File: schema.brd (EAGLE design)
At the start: 51.7 x 53.3 mm, 6 parts

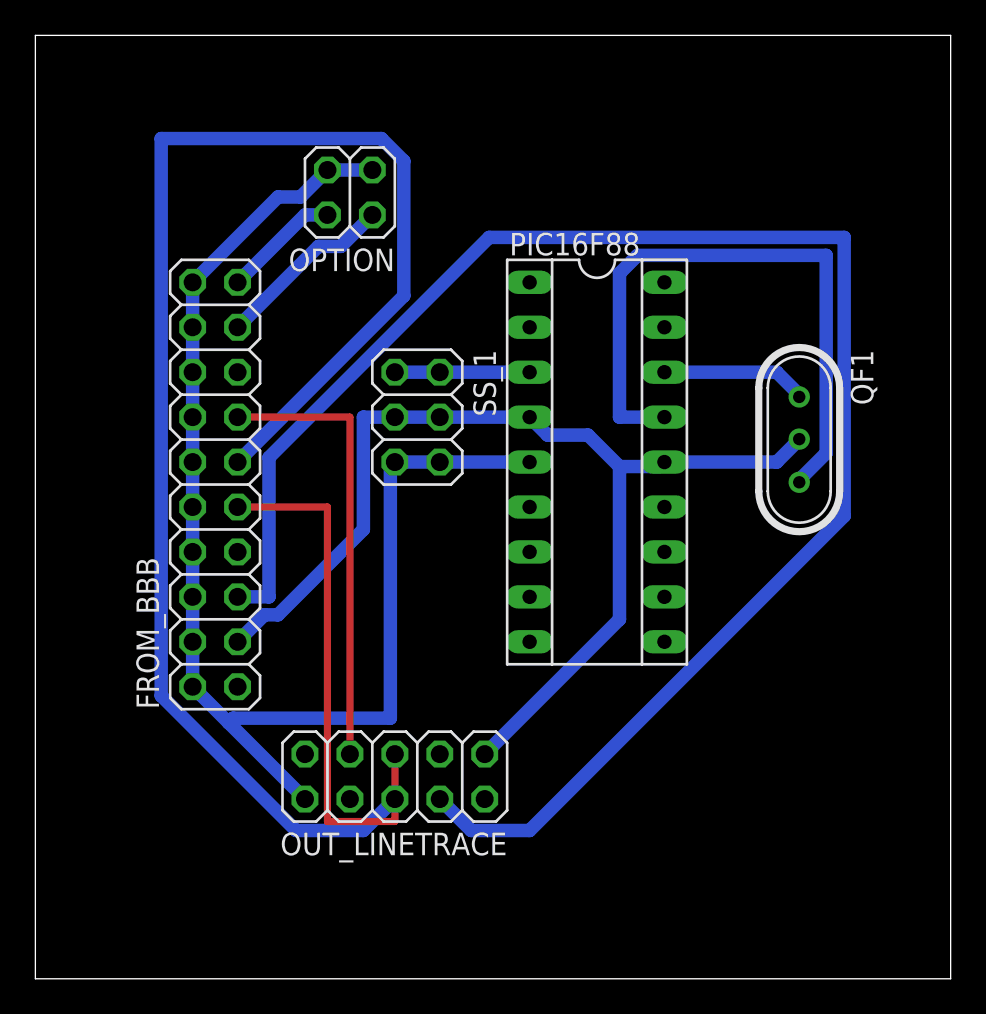
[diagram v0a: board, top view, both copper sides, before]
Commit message: trimmed the corners
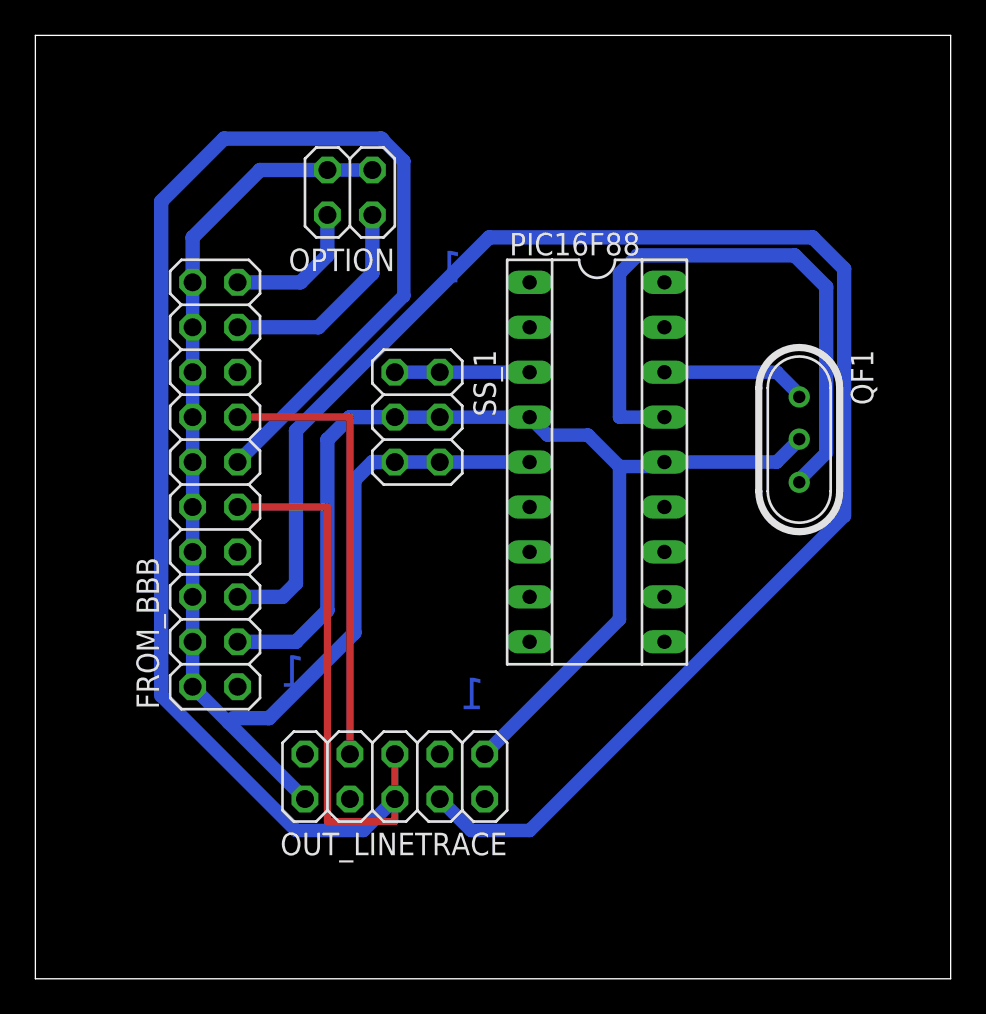
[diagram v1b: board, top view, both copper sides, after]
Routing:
- net N$3: track 83.7 -> 81.7 mm
- net N$6: track 62.0 -> 63.9 mm
- net N$10: track 10.3 -> 12.2 mm
- net GND: track 76.1 -> 74.3 mm
- net N$11: track 6.66 -> 8.00 mm
- net N$8: track 36.2 -> 35.2 mm
- net N$1: track 94.0 -> 93.4 mm
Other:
- board text added: "1"
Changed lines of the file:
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@@
 <setting verticaltext="up"/>
 </settings>
-<grid distance="0.05" unitdist="inch" unit="inch" style="dots" multiple="1" display="yes" altdistance="0.025" altunitdist="inch" altunit="inch"/>
+<grid distance="0.01" unitdist="inch" unit="inch" style="lines" multiple="1" display="yes" altdistance="0.025" altunitdist="inch" altunit="inch"/>
 <layers>
 <layer number="1" name="Top" color="4" fill="1" visible="yes" active="yes"/>
@@
 <wire x1="51.74" y1="53.33" x2="0" y2="53.33" width="0" layer="20"/>
 <wire x1="0" y1="53.33" x2="0" y2="0" width="0" layer="20"/>
+<text x="25.4" y="15.24" size="1.778" layer="16" rot="MR0">1</text>
+<text x="15.24" y="16.51" size="1.778" layer="16" rot="MR0">1</text>
+<text x="24.13" y="39.37" size="1.778" layer="16" rot="MR0">1</text>
 </plain>
 <attributes>
@@
 <wire x1="27.94" y1="8.382" x2="24.638" y2="8.382" width="0.762" layer="16"/>
 <wire x1="45.72" y1="26.162" x2="27.94" y2="8.382" width="0.762" layer="16"/>
-<wire x1="45.72" y1="41.91" x2="45.72" y2="26.162" width="0.762" layer="16"/>
-<wire x1="25.654" y1="41.91" x2="45.72" y2="41.91" width="0.762" layer="16"/>
-<wire x1="13.208" y1="29.464" x2="25.654" y2="41.91" width="0.762" layer="16"/>
-<wire x1="13.208" y1="21.59" x2="13.208" y2="29.464" width="0.762" layer="16"/>
-<wire x1="11.43" y1="21.59" x2="13.208" y2="21.59" width="0.762" layer="16"/>
+<wire x1="11.43" y1="21.59" x2="13.97" y2="21.59" width="0.8128" layer="16"/>
+<wire x1="13.97" y1="21.59" x2="14.732" y2="22.352" width="0.8128" layer="16"/>
+<wire x1="14.732" y1="22.352" x2="14.732" y2="30.988" width="0.8128" layer="16"/>
+<wire x1="14.732" y1="30.988" x2="25.654" y2="41.91" width="0.8128" layer="16"/>
+<wire x1="25.654" y1="41.91" x2="43.942" y2="41.91" width="0.8128" layer="16"/>
+<wire x1="43.942" y1="41.91" x2="45.72" y2="40.132" width="0.8128" layer="16"/>
+<wire x1="45.72" y1="40.132" x2="45.72" y2="26.162" width="0.8128" layer="16"/>
 </signal>
 <signal name="N$2">
@@
 <wire x1="14.732" y1="8.382" x2="18.542" y2="8.382" width="0.762" layer="16"/>
 <wire x1="7.112" y1="16.002" x2="14.732" y2="8.382" width="0.762" layer="16"/>
-<wire x1="7.112" y1="47.498" x2="7.112" y2="16.002" width="0.762" layer="16"/>
-<wire x1="19.558" y1="47.498" x2="7.112" y2="47.498" width="0.762" layer="16"/>
-<wire x1="20.828" y1="46.228" x2="19.558" y2="47.498" width="0.762" layer="16"/>
+<wire x1="20.828" y1="46.228" x2="19.685" y2="47.371" width="0.762" layer="16"/>
 <wire x1="20.828" y1="38.608" x2="20.828" y2="46.228" width="0.762" layer="16"/>
 <wire x1="11.43" y1="29.21" x2="20.828" y2="38.608" width="0.762" layer="16"/>
+<wire x1="7.112" y1="16.002" x2="7.112" y2="43.942" width="0.8128" layer="16"/>
+<wire x1="7.112" y1="43.942" x2="10.668" y2="47.498" width="0.8128" layer="16"/>
+<wire x1="10.668" y1="47.498" x2="19.558" y2="47.498" width="0.8128" layer="16"/>
+<wire x1="19.558" y1="47.498" x2="19.685" y2="47.371" width="0.8128" layer="16"/>
 </signal>
 <signal name="N$4">
@@
 <wire x1="8.89" y1="34.29" x2="8.89" y2="36.83" width="0.762" layer="16"/>
 <wire x1="8.89" y1="36.83" x2="8.89" y2="39.37" width="0.762" layer="16"/>
-<wire x1="14.986" y1="44.196" x2="16.51" y2="45.72" width="0.762" layer="16"/>
-<wire x1="13.716" y1="44.196" x2="14.986" y2="44.196" width="0.762" layer="16"/>
-<wire x1="8.89" y1="39.37" x2="13.716" y2="44.196" width="0.762" layer="16"/>
-<wire x1="20.066" y1="14.732" x2="20.066" y2="28.956" width="0.762" layer="16"/>
-<wire x1="11.176" y1="14.732" x2="20.066" y2="14.732" width="0.762" layer="16"/>
-<wire x1="20.066" y1="28.956" x2="20.32" y2="29.21" width="0.762" layer="16"/>
 <wire x1="11.176" y1="14.732" x2="10.922" y2="14.478" width="0.762" layer="16"/>
+<wire x1="8.89" y1="39.37" x2="8.89" y2="41.91" width="0.8128" layer="16"/>
+<wire x1="8.89" y1="41.91" x2="12.7" y2="45.72" width="0.8128" layer="16"/>
+<wire x1="12.7" y1="45.72" x2="16.51" y2="45.72" width="0.8128" layer="16"/>
+<wire x1="11.176" y1="14.732" x2="13.208" y2="14.732" width="0.8128" layer="16"/>
+<wire x1="13.208" y1="14.732" x2="18.034" y2="19.558" width="0.8128" layer="16"/>
+<wire x1="18.034" y1="19.558" x2="18.034" y2="28.194" width="0.8128" layer="16"/>
+<wire x1="18.034" y1="28.194" x2="19.05" y2="29.21" width="0.8128" layer="16"/>
+<wire x1="19.05" y1="29.21" x2="20.32" y2="29.21" width="0.8128" layer="16"/>
 </signal>
 <signal name="N$6">
@@
 <contactref element="SS_1" pad="3"/>
 <wire x1="22.86" y1="31.75" x2="27.94" y2="31.75" width="0.762" layer="16"/>
-<wire x1="12.954" y1="20.574" x2="11.43" y2="19.05" width="0.762" layer="16"/>
-<wire x1="13.716" y1="20.574" x2="12.954" y2="20.574" width="0.762" layer="16"/>
-<wire x1="18.542" y1="25.4" x2="13.716" y2="20.574" width="0.762" layer="16"/>
-<wire x1="18.542" y1="31.75" x2="18.542" y2="25.4" width="0.762" layer="16"/>
-<wire x1="20.32" y1="31.75" x2="18.542" y2="31.75" width="0.762" layer="16"/>
 <wire x1="20.32" y1="31.75" x2="22.86" y2="31.75" width="0.762" layer="16"/>
 <wire x1="41.91" y1="29.21" x2="43.18" y2="30.48" width="0.762" layer="16"/>
@@
 <wire x1="31.242" y1="30.734" x2="28.956" y2="30.734" width="0.762" layer="16"/>
 <wire x1="33.02" y1="28.956" x2="31.242" y2="30.734" width="0.762" layer="16"/>
+<wire x1="11.43" y1="19.05" x2="14.732" y2="19.05" width="0.8128" layer="16"/>
+<wire x1="14.732" y1="19.05" x2="16.51" y2="20.828" width="0.8128" layer="16"/>
+<wire x1="16.51" y1="20.828" x2="16.51" y2="30.48" width="0.8128" layer="16"/>
+<wire x1="16.51" y1="30.48" x2="17.78" y2="31.75" width="0.8128" layer="16"/>
+<wire x1="17.78" y1="31.75" x2="20.32" y2="31.75" width="0.8128" layer="16"/>
 </signal>
 <signal name="N$7">
@@
 <contactref element="QF1" pad="3"/>
 <wire x1="44.704" y1="29.718" x2="43.18" y2="28.194" width="0.762" layer="16"/>
-<wire x1="44.704" y1="40.894" x2="44.704" y2="29.718" width="0.762" layer="16"/>
-<wire x1="34.036" y1="40.894" x2="44.704" y2="40.894" width="0.762" layer="16"/>
 <wire x1="33.02" y1="39.878" x2="34.036" y2="40.894" width="0.762" layer="16"/>
 <wire x1="33.02" y1="31.75" x2="33.02" y2="39.878" width="0.762" layer="16"/>
 <wire x1="35.56" y1="31.75" x2="33.02" y2="31.75" width="0.762" layer="16"/>
 <wire x1="43.18" y1="28.194" x2="43.18" y2="28.067" width="0.762" layer="16"/>
+<wire x1="34.036" y1="40.894" x2="42.926" y2="40.894" width="0.8128" layer="16"/>
+<wire x1="42.926" y1="40.894" x2="44.704" y2="39.116" width="0.8128" layer="16"/>
+<wire x1="44.704" y1="39.116" x2="44.704" y2="29.718" width="0.8128" layer="16"/>
 </signal>
 <signal name="N$5">
@@
 <contactref element="FROM_BBB" pad="17"/>
 <contactref element="OPTION" pad="2"/>
-<wire x1="16.002" y1="41.402" x2="11.43" y2="36.83" width="0.762" layer="16"/>
-<wire x1="17.272" y1="41.402" x2="16.002" y2="41.402" width="0.762" layer="16"/>
-<wire x1="19.05" y1="43.18" x2="17.272" y2="41.402" width="0.762" layer="16"/>
+<wire x1="11.43" y1="36.83" x2="16.002" y2="36.83" width="0.8128" layer="16"/>
+<wire x1="16.002" y1="36.83" x2="19.05" y2="39.878" width="0.8128" layer="16"/>
+<wire x1="19.05" y1="39.878" x2="19.05" y2="43.18" width="0.8128" layer="16"/>
 </signal>
 <signal name="N$11">
 <contactref element="FROM_BBB" pad="19"/>
 <contactref element="OPTION" pad="4"/>
-<wire x1="15.24" y1="43.18" x2="11.43" y2="39.37" width="0.762" layer="16"/>
-<wire x1="16.51" y1="43.18" x2="15.24" y2="43.18" width="0.762" layer="16"/>
+<wire x1="11.43" y1="39.37" x2="14.986" y2="39.37" width="0.8128" layer="16"/>
+<wire x1="14.986" y1="39.37" x2="16.51" y2="40.894" width="0.8128" layer="16"/>
+<wire x1="16.51" y1="40.894" x2="16.51" y2="43.18" width="0.8128" layer="16"/>
 </signal>
 </signals>

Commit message: add PDFs and correct wrong wiring from Crystal Generator to SYS_5V
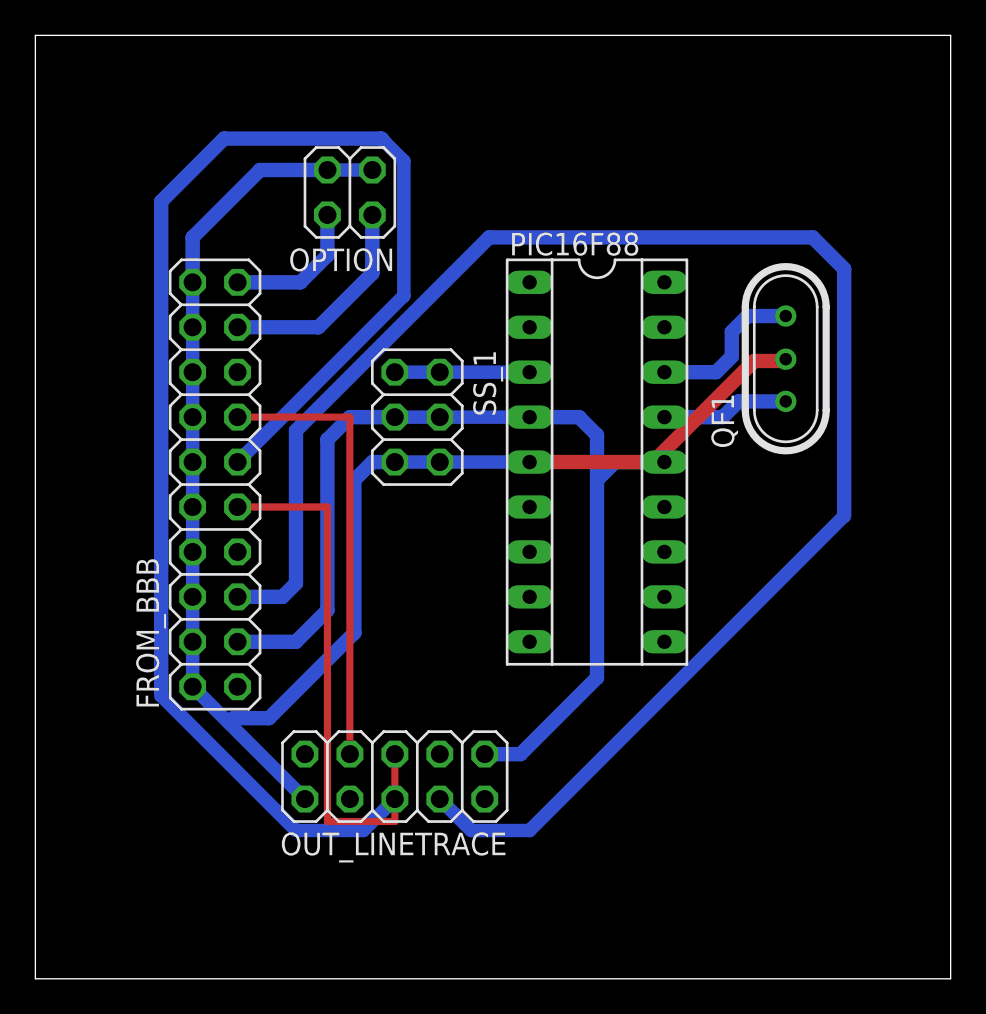
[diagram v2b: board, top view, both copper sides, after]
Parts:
- moved QF1 4.64 mm to (42.4, 35.1), turned to 90 degrees
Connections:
- net GND: now also QF1.2
- net N$6: no longer QF1.2
- net N$7: now also PIC16F88.15; no longer PIC16F88.16
- net N$8: now also PIC16F88.16; no longer PIC16F88.15
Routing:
- net N$8: track 35.2 -> 8.99 mm
- net GND: track 74.3 -> 91.2 mm
- net N$6: track 63.9 -> 58.1 mm
- net N$7: track 8.27 -> 7.23 mm
